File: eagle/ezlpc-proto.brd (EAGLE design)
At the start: 38.1 x 20.3 mm, 61 parts, among them J1 MICRO USB, Q1 12Mhz, T1 MMBT3906, U1 PRTR5V0U2X, U2 MIC5225-3.3v, U3 LPC11U35FHI33/501, U4 BAS40-05

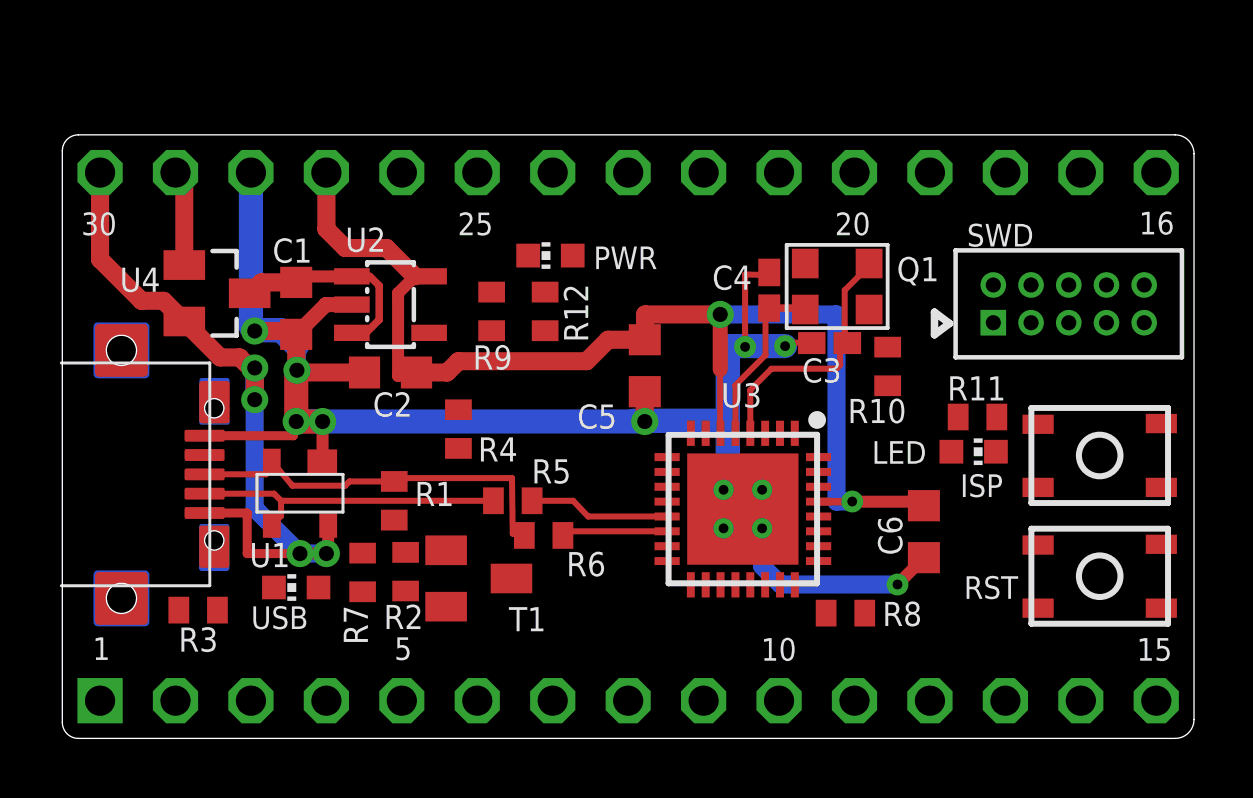
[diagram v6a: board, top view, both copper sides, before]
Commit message: Tweaked the silk screen layer.
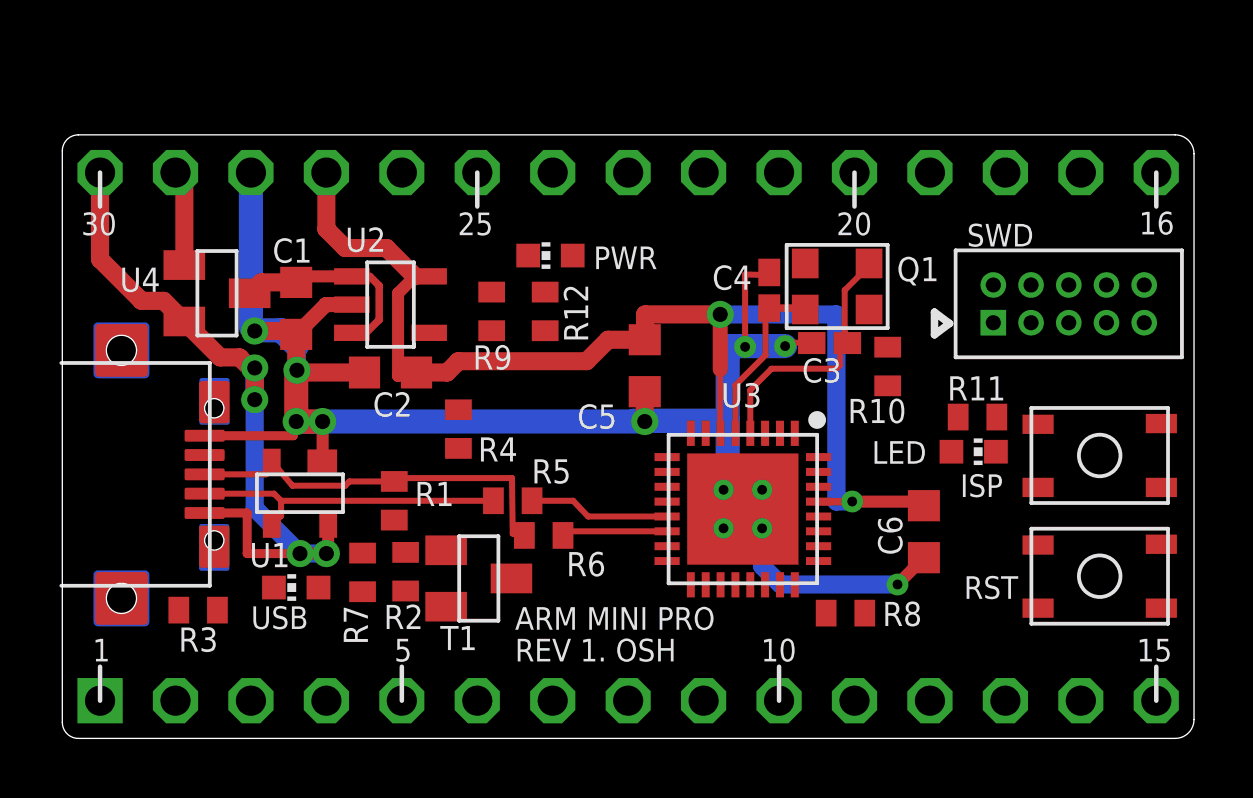
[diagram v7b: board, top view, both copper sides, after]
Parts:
- C1, C2, C5, C6: device ezlpc-proto:CAPACITOR-0603K -> ezlpc-proto:C0603K
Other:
- board text added: "ARM MINI PRO"
- board text added: "REV 1. OSH"
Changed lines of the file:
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@@
 <setting verticaltext="up"/>
 </settings>
-<grid distance="1" unitdist="mil" unit="mil" style="lines" multiple="1" display="yes" altdistance="1" altunitdist="mil" altunit="mil"/>
+<grid distance="50" unitdist="mil" unit="mil" style="lines" multiple="1" display="yes" altdistance="1" altunitdist="mil" altunit="mil"/>
 <layers>
 <layer number="1" name="Top" color="4" fill="1" visible="yes" active="yes"/>
@@
 <text x="27.2542" y="9.2456" size="0.762" layer="21" font="vector" ratio="10">LED</text>
 <text x="6.35" y="3.683" size="0.762" layer="21" font="vector" ratio="10">USB</text>
-<text x="1.016" y="2.6416" size="0.762" layer="21" font="vector" ratio="10">1</text>
-<text x="11.176" y="2.6416" size="0.762" layer="21" font="vector" ratio="10">5</text>
-<text x="23.5204" y="2.6162" size="0.762" layer="21" font="vector" ratio="10">10</text>
-<text x="36.1696" y="2.6162" size="0.762" layer="21" font="vector" ratio="10">15</text>
+<text x="1.016" y="2.5908" size="0.762" layer="21" font="vector" ratio="10">1</text>
+<text x="11.176" y="2.5908" size="0.762" layer="21" font="vector" ratio="10">5</text>
+<text x="23.5204" y="2.5908" size="0.762" layer="21" font="vector" ratio="10">10</text>
+<text x="36.1696" y="2.5908" size="0.762" layer="21" font="vector" ratio="10">15</text>
 <text x="36.2458" y="16.9672" size="0.762" layer="21" font="vector" ratio="10">16</text>
-<text x="26.0096" y="16.9418" size="0.762" layer="21" font="vector" ratio="10">20</text>
+<text x="26.0604" y="16.9418" size="0.762" layer="21" font="vector" ratio="10">20</text>
 <text x="13.3096" y="16.9418" size="0.762" layer="21" font="vector" ratio="10">25</text>
 <text x="0.635" y="16.9418" size="0.762" layer="21" font="vector" ratio="10">30</text>
 <text x="30.4546" y="16.5608" size="0.762" layer="21" font="vector" ratio="10">SWD</text>
+<text x="15.24" y="3.6576" size="0.762" layer="21" font="vector" ratio="10">ARM MINI PRO</text>
+<text x="15.24" y="2.5908" size="0.762" layer="21" font="vector" ratio="10">REV 1. OSH</text>
+<wire x1="1.27" y1="2.413" x2="1.27" y2="1.27" width="0.1524" layer="21"/>
+<wire x1="11.43" y1="2.413" x2="11.43" y2="1.27" width="0.1524" layer="21"/>
+<wire x1="24.13" y1="2.413" x2="24.13" y2="1.27" width="0.1524" layer="21"/>
+<wire x1="36.83" y1="2.413" x2="36.83" y2="1.27" width="0.1524" layer="21"/>
+<wire x1="26.67" y1="17.907" x2="26.67" y2="19.05" width="0.1524" layer="21"/>
+<wire x1="36.83" y1="17.907" x2="36.83" y2="19.05" width="0.1524" layer="21"/>
+<wire x1="13.97" y1="17.907" x2="13.97" y2="19.05" width="0.1524" layer="21"/>
+<wire x1="1.27" y1="17.907" x2="1.27" y2="19.05" width="0.1524" layer="21"/>
 </plain>
 <attributes>
@@
 <attribute name="VALUE" x="7.62" y="16.51" size="1.27" layer="27" rot="R270"/>
 </element>
-<element name="C2" library="ezlpc-proto" package="CAPACITOR-0603K" value="2u2" x="11.049" y="12.319" smashed="yes" rot="R180">
+<element name="C2" library="ezlpc-proto" package="C0603K" value="2u2" x="11.049" y="12.319" smashed="yes" rot="R180">
 <attribute name="NAME" x="10.4522" y="10.8354" size="0.8128" layer="25" font="vector" ratio="10"/>
 <attribute name="VALUE" x="11.849" y="13.969" size="1.016" layer="27" rot="R180"/>
 </element>
-<element name="C1" library="ezlpc-proto" package="CAPACITOR-0603K" value="2u2" x="7.874" y="14.478" smashed="yes" rot="R270">
+<element name="C1" library="ezlpc-proto" package="C0603K" value="2u2" x="7.874" y="14.478" smashed="yes" rot="R270">
 <attribute name="NAME" x="7.074" y="16.017" size="0.8128" layer="25" font="vector" ratio="10"/>
 <attribute name="VALUE" x="6.224" y="15.278" size="1.016" layer="27" rot="R270"/>
@@
 <attribute name="VALUE" x="25.2498" y="14.5876" size="1.016" layer="27" rot="R90"/>
 </element>
-<element name="C6" library="ezlpc-proto" package="CAPACITOR-0603K" value="0.1uF" x="29.0068" y="6.9596" smashed="yes" rot="R270">
+<element name="C6" library="ezlpc-proto" package="C0603K" value="0.1uF" x="29.0068" y="6.9596" smashed="yes" rot="R270">
 <attribute name="NAME" x="28.2806" y="6.1596" size="0.8128" layer="25" font="vector" ratio="10" rot="R90"/>
 <attribute name="VALUE" x="27.3568" y="7.7596" size="1.016" layer="27" rot="R270"/>
 </element>
-<element name="C5" library="ezlpc-proto" package="CAPACITOR-0603K" value="0.1uF" x="19.6088" y="12.5476" smashed="yes" rot="R270">
+<element name="C5" library="ezlpc-proto" package="C0603K" value="0.1uF" x="19.6088" y="12.5476" smashed="yes" rot="R270">
 <attribute name="NAME" x="17.3356" y="10.429" size="0.8128" layer="25" font="vector" ratio="10"/>
 <attribute name="VALUE" x="17.9588" y="13.3476" size="1.016" layer="27" rot="R270"/>
@@
 </element>
 <element name="T1" library="ezlpc-proto" package="SOT23-BEC" value="MMBT3906" x="14.0208" y="5.3848" smashed="yes" rot="R270">
-<attribute name="NAME" x="15.0368" y="3.6068" size="0.8128" layer="25" font="vector" ratio="10"/>
+<attribute name="NAME" x="12.7254" y="2.9718" size="0.8128" layer="25" font="vector" ratio="10"/>
 <attribute name="VALUE" x="10.8458" y="7.2898" size="1.27" layer="27" rot="R270"/>
 </element>

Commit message: Cleaned up ERC warnings.
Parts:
- J2: value (none) -> SWD HEADER
- TP1, TP10, TP11, TP12, TP13, TP14, TP15, TP16, TP17, TP18, TP19, TP2, TP20, TP21, TP22, TP23, TP24, TP25, TP26, TP27, TP28, TP29, TP3, TP30, TP4, TP5, TP6, TP7, TP8, TP9: value (none) -> HDR1
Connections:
- net AUX-VIN renamed EXT-VIN
- removed net N$11: J2.8
- removed net PIO0_9: TP5.1, U3.18
- net PIO0_9-SWDO: now also TP5.1, U3.18
